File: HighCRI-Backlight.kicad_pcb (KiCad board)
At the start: 2 copper layers, 100 x 100 mm, 119 parts, among them J1 Conn_01x03, J2 Screw_Terminal_01x02, J3 Screw_Terminal_01x02, Q1 AOD4130, Q2 AOD4130, Q3 AOD4130, U1 L78L24_SO8, U2 LM324

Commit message: Routing Seemingly Complete
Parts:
- R1: footprint Resistor_SMD:R_0603_1608Metric_Pad0.98x0.95mm_HandSolder -> Resistor_SMD:R_1206_3216Metric_Pad1.30x1.75mm_HandSolder
- moved R3 15.4 mm to (126.5, 130.5)
- moved R1 15.0 mm to (120.5, 116.5), turned to -90 degrees
- moved R9 14.7 mm to (172.6, 130.5)
- moved R6 14.6 mm to (149.5, 130.5)
- moved C6 14.2 mm to (145.5, 130.5), turned to 180 degrees
- moved C5 13.4 mm to (122.5, 130.5), turned to 180 degrees
- moved C7 13.4 mm to (168.5, 130.5), turned to 180 degrees
- moved R8 10.3 mm to (164.8, 134.9), turned to -90 degrees
- moved R2 10.2 mm to (118.8, 135.0), turned to -90 degrees
- moved R5 10.0 mm to (141.8, 135.0), turned to -90 degrees
- moved C1 6.37 mm to (112.8, 93.2)
- moved C2 6.37 mm to (108.5, 120.0)
- moved C3 6.37 mm to (108.5, 114.8)
- moved C4 6.37 mm to (112.8, 105.2)
- moved D1 6.37 mm to (125.8, 56.2)
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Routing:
- net +36V: track 0.00 -> 296.5 mm
- net Net-(C7-Pad1): track 0.00 -> 62.9 mm, vias 0 -> 2
- net Net-(C7-Pad2): track 0.00 -> 60.4 mm, vias 0 -> 2
- net Net-(C6-Pad1): track 0.00 -> 46.6 mm, vias 0 -> 2
- net Net-(C6-Pad2): track 0.00 -> 44.0 mm, vias 0 -> 2
- net +24V: track 0.00 -> 37.8 mm
- net Net-(C5-Pad1): track 0.00 -> 28.3 mm, vias 0 -> 2
- net GND: track 0.00 -> 27.1 mm, vias 0 -> 31
- net Net-(D70-Pad1): track 0.00 -> 26.2 mm
- net Net-(C5-Pad2): track 0.00 -> 26.0 mm, vias 0 -> 2
- net Net-(D40-Pad1): track 0.00 -> 26.0 mm
- net Net-(D10-Pad1): track 0.00 -> 25.7 mm
- net Net-(J1-Pad2): track 0.00 -> 25.5 mm
- net /I_SET: track 0.00 -> 14.1 mm
- net Net-(Q3-Pad3): track 0.00 -> 9.51 mm
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- added copper zone on B.Cu, net GND
- added copper zone on F.Cu, net GND

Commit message: Silkscreening
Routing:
- net GND: vias 31 -> 30
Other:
- board text added: "+"
- board text added: "-"
- board text added: "24V"
- board text added: "Designed by Clement Hathaway - April 2022"
- board text added: "GND"
- board text added: "Input"
- board text added: "Light Table"
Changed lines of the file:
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@@
     (property "Sheetname" "")
     (attr smd)
-    (fp_text reference "C5" (at 0 -1.65) (layer "F.SilkS")
+    (fp_text reference "C5" (at 2.75 0) (layer "F.SilkS")
       (effects (font (size 1 1) (thickness 0.15)))
     )
@@
     (property "Wattage" "0.5W")
     (attr smd)
-    (fp_text reference "R7" (at 0 -2.28 90) (layer "F.SilkS")
+    (fp_text reference "R7" (at -3.25 0 180) (layer "F.SilkS")
       (effects (font (size 1 1) (thickness 0.15)))
     )
@@
     (property "Sheetname" "")
     (attr smd)
-    (fp_text reference "C1" (at 0 -1.85) (layer "F.SilkS")
+    (fp_text reference "C1" (at 3.5 -0.25) (layer "F.SilkS")
       (effects (font (size 1 1) (thickness 0.15)))
     )
@@
     (property "Sheetname" "")
     (attr smd)
-    (fp_text reference "R1" (at 0 -1.82 -90) (layer "F.SilkS")
+    (fp_text reference "R1" (at -3.5 0.25) (layer "F.SilkS")
       (effects (font (size 1 1) (thickness 0.15)))
     )
@@
     (property "Sheetname" "")
     (attr through_hole)
-    (fp_text reference "J1" (at 4.385 -2.27) (layer "F.SilkS")
+    (fp_text reference "J1" (at 2.875 -2.725) (layer "F.SilkS")
       (effects (font (size 1 1) (thickness 0.15)))
     )
@@
     (property "URL" "https://www.ebay.com/itm/192840344146?epid=8029762746&_trkparms=ispr%3D1&hash=item2ce62e2252:g:AAEAAOSwyhBcddkx&amdata=enc%3AAQAGAAAA4GlQRaV0kVJ%2BfatZOiIvI7gK3jCY4e%2FgQQLNpiEjhFaS5wt6ACAGzfVbKZalcnf%2BYX%2FYSiu7kM1EHKzYB%2BCwUcN6FvfmgkV9%2BwhcBX9kZb2iHXEkM660zFg09pJ0lLRy9wkDAKMh2YVhgocE1Vc2wCZWaUbUQpQfm7y%2BEDr4qz8K%2BtV1zoigDT4n9M8C3Nn2XT22tIYjXSWXojX2qu0TTxSAmLNbx7dOM0fkCxxoXMOobFzlkODA%2BNjE9HPV35w%2BujSaQk%2B7Z5RmtYte8485yQoIIsVNSKLoozOnWVRj%2BvC%2F%7Ctkp%3ABFBMqMjFs_1f")
     (attr through_hole)
-    (fp_text reference "J3" (at 2.54 -5.08 90) (layer "F.SilkS")
+    (fp_text reference "J3" (at 2.54 -5.08 180) (layer "F.SilkS")
       (effects (font (size 1 1) (thickness 0.15)))
     )
@@
     (property "Wattage" "0.5W")
     (attr smd)
-    (fp_text reference "R4" (at 0 -2.28 90) (layer "F.SilkS")
+    (fp_text reference "R4" (at -3.25 0) (layer "F.SilkS")
       (effects (font (size 1 1) (thickness 0.15)))
     )
@@
     (property "Sheetname" "")
     (attr smd)
-    (fp_text reference "C7" (at 0 -1.65) (layer "F.SilkS")
+    (fp_text reference "C7" (at 2.75 0) (layer "F.SilkS")
       (effects (font (size 1 1) (thickness 0.15)))
     )
@@
     (property "Sheetname" "")
     (attr smd)
-    (fp_text reference "C4" (at 0 -1.85) (layer "F.SilkS")
+    (fp_text reference "C4" (at -3.5 0.25) (layer "F.SilkS")
       (effects (font (size 1 1) (thickness 0.15)))
     )
@@
     (property "Sheetname" "")
     (attr smd)
-    (fp_text reference "R8" (at 0 -1.43 90) (layer "F.SilkS")
+    (fp_text reference "R8" (at 2.5875 0 180) (layer "F.SilkS")
       (effects (font (size 1 1) (thickness 0.15)))
     )
@@
     (property "Sheetname" "")
     (attr smd)
-    (fp_text reference "C3" (at 0 -1.85 90) (layer "F.SilkS")
+    (fp_text reference "C3" (at 3.25 -1.25 180) (layer "F.SilkS")
       (effects (font (size 1 1) (thickness 0.15)))
     )
@@
     (property "Sheetname" "")
     (attr smd)
-    (fp_text reference "R2" (at 0 -1.43 90) (layer "F.SilkS")
+    (fp_text reference "R2" (at 2.5 0 180) (layer "F.SilkS")
       (effects (font (size 1 1) (thickness 0.15)))
     )
@@
     (property "Sheetname" "")
     (attr smd)
-    (fp_text reference "C2" (at 0 -1.85 90) (layer "F.SilkS")
+    (fp_text reference "C2" (at -3.5 -1.25 180) (layer "F.SilkS")
       (effects (font (size 1 1) (thickness 0.15)))
     )
@@
     (property "Wattage" "0.5W")
     (attr smd)
-    (fp_text reference "R10" (at 0 -2.28 90) (layer "F.SilkS")
+    (fp_text reference "R10" (at -3.25 0 180) (layer "F.SilkS")
       (effects (font (size 1 1) (thickness 0.15)))
     )
@@
     (property "Sheetname" "")
     (attr smd)
-    (fp_text reference "C6" (at 0 -1.65) (layer "F.SilkS")
+    (fp_text reference "C6" (at 2.75 0) (layer "F.SilkS")
       (effects (font (size 1 1) (thickness 0.15)))
     )
@@
     (property "Sheetname" "")
     (attr smd)
-    (fp_text reference "U1" (at 0 -3.4 90) (layer "F.SilkS")
+    (fp_text reference "U1" (at 0 -4 180) (layer "F.SilkS")
       (effects (font (size 1 1) (thickness 0.15)))
     )
@@
     (property "Sheetname" "")
     (attr smd)
-    (fp_text reference "R5" (at 0 -1.43 90) (layer "F.SilkS")
+    (fp_text reference "R5" (at 2.5 0 180) (layer "F.SilkS")
       (effects (font (size 1 1) (thickness 0.15)))
     )
@@
     (property "URL" "https://www.ebay.com/itm/192840344146?epid=8029762746&_trkparms=ispr%3D1&hash=item2ce62e2252:g:AAEAAOSwyhBcddkx&amdata=enc%3AAQAGAAAA4GlQRaV0kVJ%2BfatZOiIvI7gK3jCY4e%2FgQQLNpiEjhFaS5wt6ACAGzfVbKZalcnf%2BYX%2FYSiu7kM1EHKzYB%2BCwUcN6FvfmgkV9%2BwhcBX9kZb2iHXEkM660zFg09pJ0lLRy9wkDAKMh2YVhgocE1Vc2wCZWaUbUQpQfm7y%2BEDr4qz8K%2BtV1zoigDT4n9M8C3Nn2XT22tIYjXSWXojX2qu0TTxSAmLNbx7dOM0fkCxxoXMOobFzlkODA%2BNjE9HPV35w%2BujSaQk%2B7Z5RmtYte8485yQoIIsVNSKLoozOnWVRj%2BvC%2F%7Ctkp%3ABFBMqMjFs_1f")
     (attr through_hole)
-    (fp_text reference "J2" (at 2.54 -5.08 90) (layer "F.SilkS")
+    (fp_text reference "J2" (at 2.54 -5.08 180) (layer "F.SilkS")
       (effects (font (size 1 1) (thickness 0.15)))
     )
@@
   (gr_line (start 105.75 52.25) (end 105.75 142.25) (layer "Edge.Cuts") (width 0.1))
   (gr_line (start 110.75 47.25) (end 200.75 47.25) (layer "Edge.Cuts") (width 0.1))
+  (gr_text "GND" (at 113.25 133.775) (layer "F.SilkS")
+    (effects (font (size 1 1) (thickness 0.15)) (justify left))
+  )
+  (gr_text "-" (at 192.75 130.5) (layer "F.SilkS")
+    (effects (font (size 5 5) (thickness 0.15)))
+  )
+  (gr_text "24V" (at 113.25 128.5) (layer "F.SilkS")
+    (effects (font (size 1 1) (thickness 0.15)) (justify left))
+  )
+  (gr_text "+" (at 192.75 119.5) (layer "F.SilkS")
+    (effects (font (size 5 5) (thickness 0.15)))
+  )
+  (gr_text "Input" (at 113.25 131) (layer "F.SilkS")
+    (effects (font (size 1 1) (thickness 0.15)) (justify left))
+  )
+  (gr_text "Designed by Clement Hathaway - April 2022" (at 155.75 50.5) (layer "F.SilkS")
+    (effects (font (size 1 1) (thickness 0.15)))
+  )
+  (gr_text "Light Table" (at 199.75 86.5 90) (layer "F.SilkS")
+    (effects (font (size 5 5) (thickness 0.3)))
+  )
   (segment (start 113.115 96.775) (end 114.385 96.775) (width 0.5) (layer "F.Cu") (net 1))
   (segment (start 108.5 111.5) (end 108.75 111.25) (width 0.75) (layer "F.Cu") (net 1))
@@
   (via (at 108.75 123.25) (size 1.6) (drill 0.8) (layers "F.Cu" "B.Cu") (net 1))
   (via (at 118.25 68) (size 1.6) (drill 0.8) (layers "F.Cu" "B.Cu") (free) (net 1))
-  (via (at 193.25 120.5) (size 1.6) (drill 0.8) (layers "F.Cu" "B.Cu") (free) (net 1))
   (via (at 193.25 143) (size 1.6) (drill 0.8) (layers "F.Cu" "B.Cu") (free) (net 1))
   (via (at 118.25 90.5) (size 1.6) (drill 0.8) (layers "F.Cu" "B.Cu") (free) (net 1))

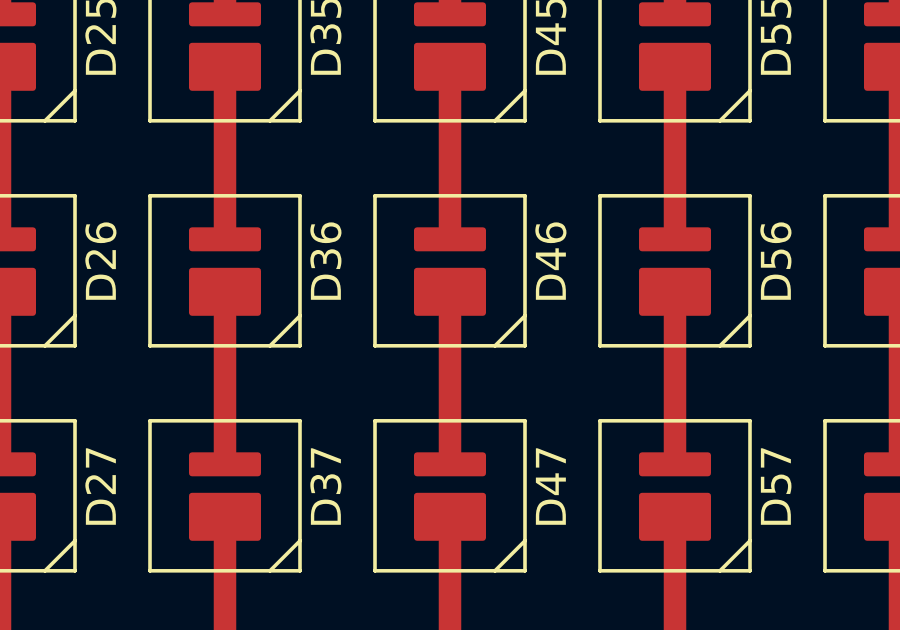
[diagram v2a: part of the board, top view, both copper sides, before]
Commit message: Added lightbulb symbol to back
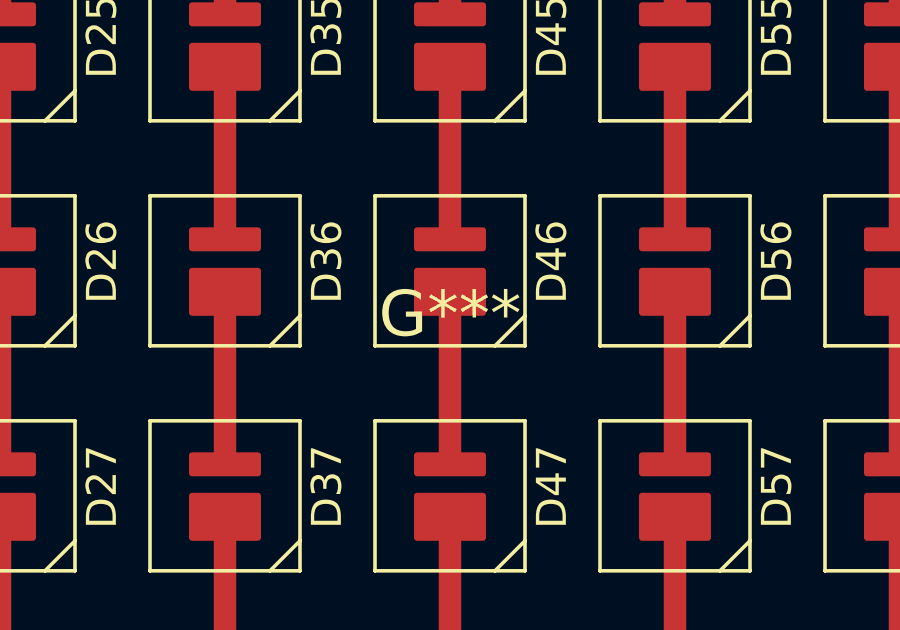
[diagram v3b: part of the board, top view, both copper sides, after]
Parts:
- added G***: LOGO, LOGO, B.Cu at (155.8, 95.5)
